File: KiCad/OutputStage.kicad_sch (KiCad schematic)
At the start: 42 parts, among them J2 Conn_Coaxial, Q1 BD135, Q2 BD136, U6 LM318H

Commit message: Tidied up schematic, changed footprints
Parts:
- R35: footprint Potentiometer_THT:Potentiometer_ACP_CA9-V10_Vertical -> Potentiometer_SMD:Potentiometer_Bourns_TC33X_Vertical
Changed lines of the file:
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@@
 			)
 		)
-		(property "Footprint" "Potentiometer_THT:Potentiometer_ACP_CA9-V10_Vertical"
+		(property "Footprint" "Potentiometer_SMD:Potentiometer_Bourns_TC33X_Vertical"
 			(at 160.782 113.03 90)
 			(effects

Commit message: Alfa version of PCB design
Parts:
- added C18, C19: 100n, Capacitor_SMD:C_0805_2012Metric_Pad1.18x1.45mm_HandSolder, symbol Device:C
- added C2, C4: 100u, Capacitor_THT:CP_Radial_D5.0mm_P2.50mm, symbol Device:C_Polarized
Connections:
- net +10V: now also C18.1, C2.1
- net -10V: now also C19.2, C4.2
- net GND: now also C18.2, C19.1, C2.2, C4.1
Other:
- note added: "AB Amp Power"
- moved on the sheet: C15, C16

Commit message: PCB design
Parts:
- added R39, R40: 100, Resistor_SMD:R_0805_2012Metric_Pad1.20x1.40mm_HandSolder, symbol Device:R
- R37: renamed from R35; value 100 -> 1k
- renumbered C14 to C13, C15 to C14, C16 to C15, C18 to C16, C19 to C17, C2 to C18, C4 to C19, D3 to D7, D4 to D8, R8 to R10, R9 to R11, R10 to R12, R11 to R13, R12 to R14, R13 to R15, R14 to R16, R15 to R17, R16 to R18, R17 to R19, R18 to R20, R19 to R21, R20 to R22, R21 to R23, R22 to R24, R23 to R25, R24 to R26, R25 to R27, R26 to R28, R27 to R29, R28 to R30, R29 to R31, R30 to R32, R31 to R33, R32 to R34, R33 to R35, R34 to R36, R36 to R38, R37 to R41, R38 to R42, R6 to R8, R7 to R9
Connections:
- net at D7.1 (K), R35.2, R37.1: now also R39.2
- net at D8.2 (A), R37.2: now also R40.1
- new net: R39.1, R40.2
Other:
- moved on the sheet: D8

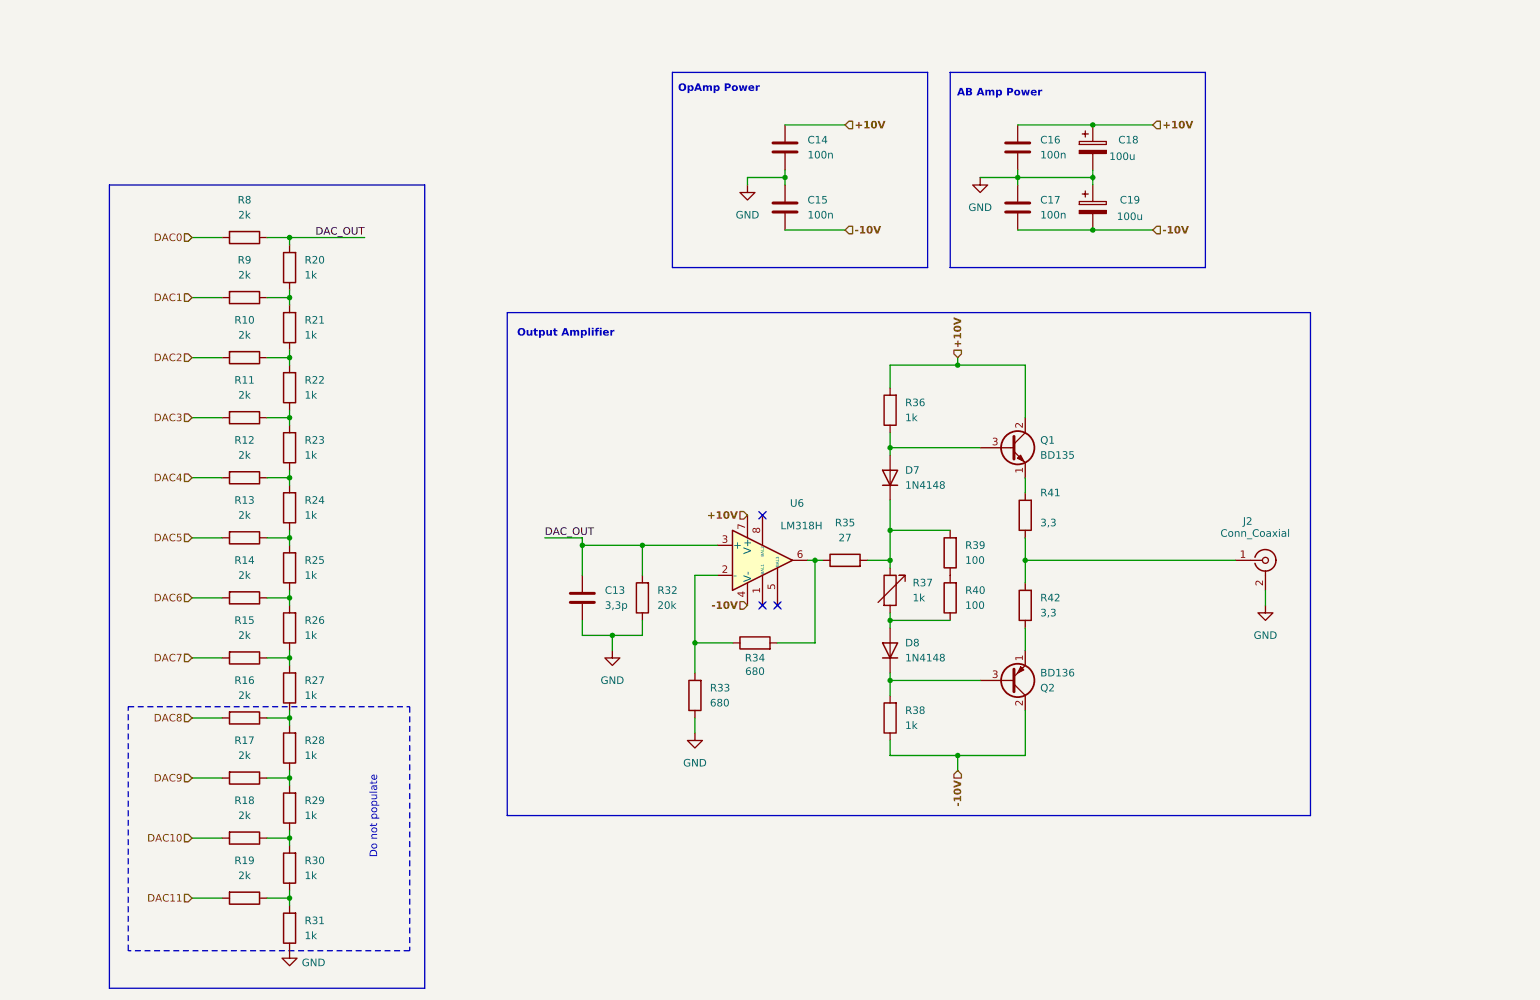
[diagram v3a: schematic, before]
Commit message: output sim, filter sim, filter sch, output change
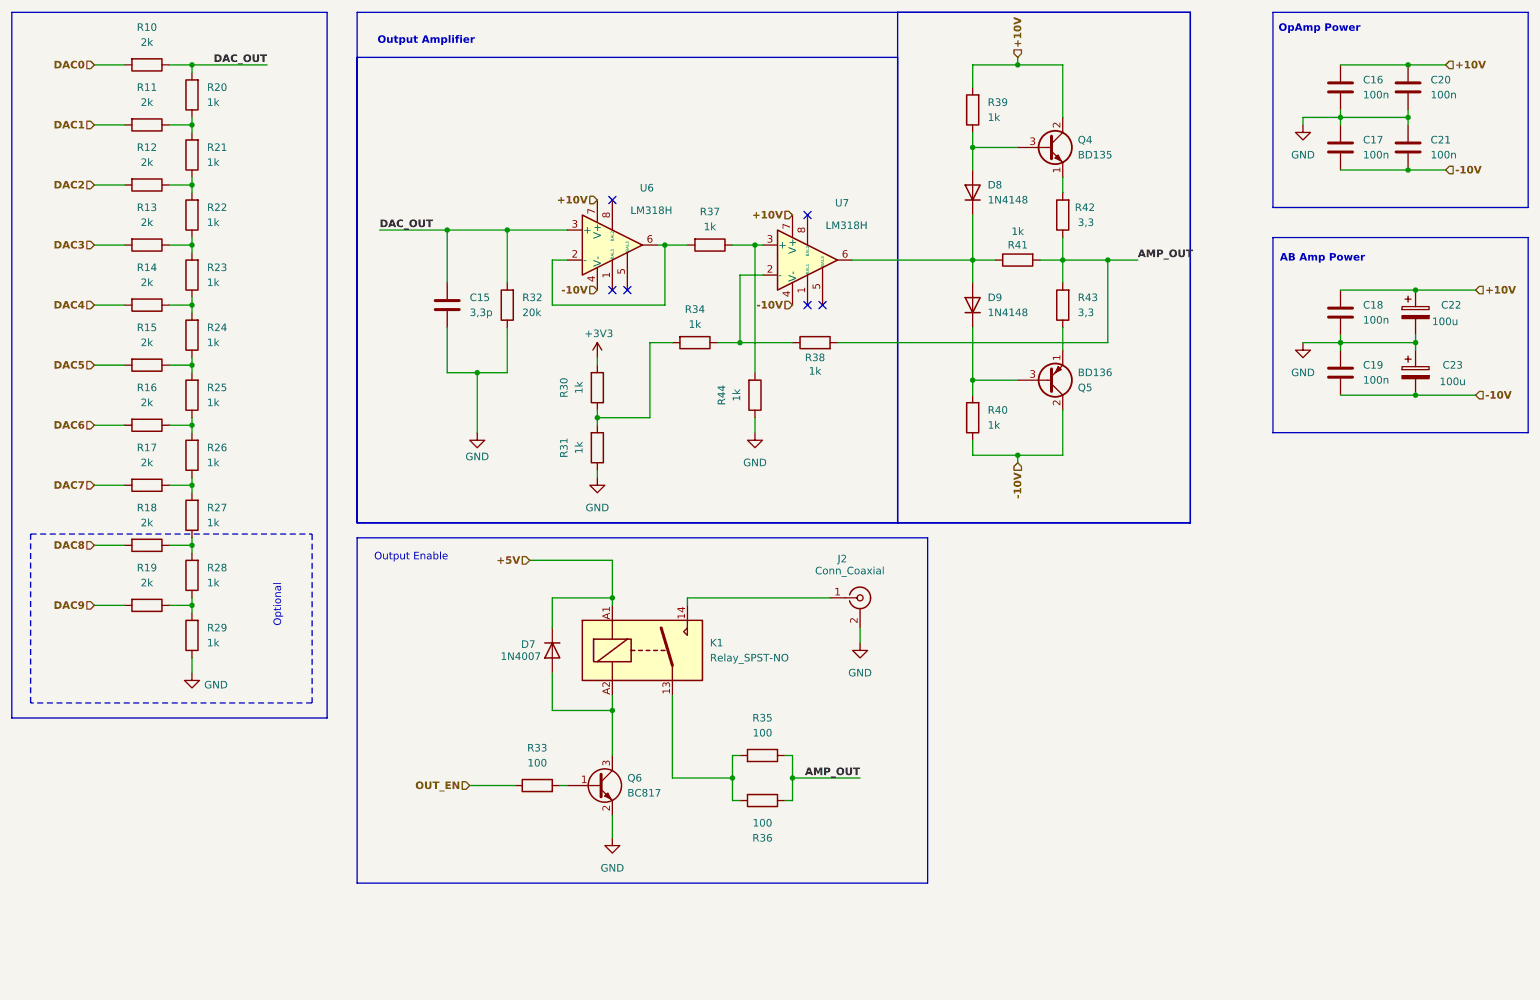
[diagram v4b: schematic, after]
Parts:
- removed R18, R19: 2k, Resistor_SMD:R_0805_2012Metric_Pad1.20x1.40mm_HandSolder, symbol Device:R
- removed R37: 1k, Potentiometer_SMD:Potentiometer_Bourns_TC33X_Vertical, symbol Device:R_Variable
- removed R39, R40: 100, Resistor_SMD:R_0805_2012Metric_Pad1.20x1.40mm_HandSolder, symbol Device:R
- added C20, C21: 100n, Capacitor_SMD:C_0805_2012Metric_Pad1.18x1.45mm_HandSolder, symbol Device:C
- added D7: 1N4007, Diode_SMD:D_SOD-123F, symbol Diode:1N4007
- added K1: Relay_SPST-NO, symbol Relay:Relay_SPST-NO
- added Q6: BC817, Package_TO_SOT_SMD:SOT-23_Handsoldering, symbol Transistor_BJT:BC817
- added R34, R37, R41, R44: 1k, Resistor_SMD:R_0805_2012Metric_Pad1.20x1.40mm_HandSolder, symbol Device:R
- added R36: 100, symbol Device:R
- added U6: LM318H, Package_DIP:DIP-8_W7.62mm, symbol Amplifier_Operational:LM318H
- R33: value 680 -> 100; footprint Resistor_SMD:R_0805_2012Metric_Pad1.20x1.40mm_HandSolder -> (none)
- R35: value 27 -> 100; footprint Resistor_SMD:R_0805_2012Metric_Pad1.20x1.40mm_HandSolder -> (none)
- R38: renamed from R34; value 680 -> 1k
- renumbered C13 to C15, C14 to C16, C15 to C17, C16 to C18, C17 to C19, C18 to C22, C19 to C23, D7 to D8, D8 to D9, Q1 to Q4, Q2 to Q5, R8 to R10, R9 to R11, R10 to R12, R11 to R13, R12 to R14, R13 to R15, R14 to R16, R15 to R17, R16 to R18, R17 to R19, R36 to R39, R38 to R40, R41 to R42, R42 to R43, U6 to U7
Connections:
- net +10V: now also C20.1, U6.7 (V+)
- net -10V: now also C21.2, U6.4 (V-)
- net DAC_OUT: now also U6.3 (+); no longer U7.3 (+)
- net GND: now also R29.1, C20.2, C21.1, Q6.2 (E), R44.1; no longer R33.1
- net AMP_OUT: now reaches R42.1, R43.2
- net AMP_OUT: now also R35.1, R38.2, R36.1, R41.2; no longer J2.1 (In)
- net at D8.1 (K): now also D9.2 (A), U7.6, R41.1; no longer R35.2
- net at R38.1, U7.2 (-): now also R34.1; no longer R33.2
- net at R30.1, R31.2: now also R34.2
- net +3V3: now reaches R30.2
- net +3V3: no longer R29.1
- new net: Q6.1 (B), R33.2
- new net: J2.1 (In), K1.14
- new net: R37.1, R44.2, U7.3 (+)
- new net: R37.2, U6.2 (-), U6.6
- new net: D7.2 (A), K1.A2, Q6.3 (C)
- new net: K1.13, R35.2, R36.2
- new net +5V: D7.1 (K), K1.A1
- new net OUT_EN: R33.1
- no-connect marks 3 -> 6
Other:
- note added: "Optional"
- note added: "Output Enable"
- note removed: "Do not populate"
- moved on the sheet: C15, C16, C17, C18, C19, C22, C23, D8, D9, J2, Q4, Q5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

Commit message: Updated footprints
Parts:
- K1: footprint (none) -> Relay_THT:Relay_SPDT_SANYOU_SRD_Series_Form_C
- R33: footprint (none) -> Resistor_SMD:R_0805_2012Metric_Pad1.20x1.40mm_HandSolder
- R35, R36: footprint (none) -> Resistor_SMD:R_2512_6332Metric_Pad1.40x3.35mm_HandSolder
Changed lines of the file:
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@@
 			)
 		)
-		(property "Footprint" ""
+		(property "Footprint" "Resistor_SMD:R_0805_2012Metric_Pad1.20x1.40mm_HandSolder"
 			(at 102.87 147.828 90)
 			(effects
@@
 			)
 		)
-		(property "Footprint" ""
+		(property "Footprint" "Resistor_SMD:R_2512_6332Metric_Pad1.40x3.35mm_HandSolder"
 			(at 140.97 146.812 90)
 			(effects
@@
 			)
 		)
-		(property "Footprint" ""
+		(property "Footprint" "Resistor_SMD:R_2512_6332Metric_Pad1.40x3.35mm_HandSolder"
 			(at 140.97 142.748 90)
 			(effects
@@
 			)
 		)
-		(property "Footprint" ""
+		(property "Footprint" "Relay_THT:Relay_SPDT_SANYOU_SRD_Series_Form_C"
 			(at 132.08 124.46 0)
 			(effects

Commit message: Final PCB version (probably)
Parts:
- added C24: 100n, Capacitor_SMD:C_0805_2012Metric_Pad1.18x1.45mm_HandSolder, symbol Device:C
- K1: footprint Relay_THT:Relay_SPDT_SANYOU_SRD_Series_Form_C -> Relay_THT:Relay_SPST_SANYOU_SRD_Series_Form_B
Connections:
- net +5V: now also C24.1
- net AMP_OUT: now also K1.13; no longer R35.1, R36.1
- net GND: now also C24.2
- net at J2.1 (In): now also R35.1, R36.1; no longer K1.14
- net at R35.2, R36.2: now also K1.14; no longer K1.13
- net +3V3 renamed 3.3Sig
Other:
- moved on the sheet: D7, K1, R35, R36
